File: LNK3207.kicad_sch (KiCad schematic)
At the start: 18 parts, among them U1 LNK3206D

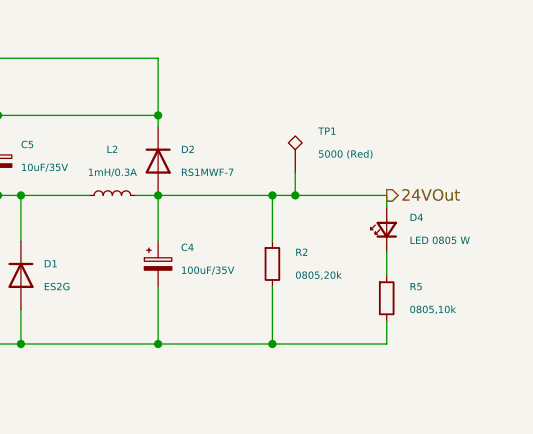
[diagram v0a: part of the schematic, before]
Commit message: [A02] Edited R4, R5
R4 20k -> 10k since nothing else uses 20k
R5 10k -> 510k to reduce D3 LED brightness
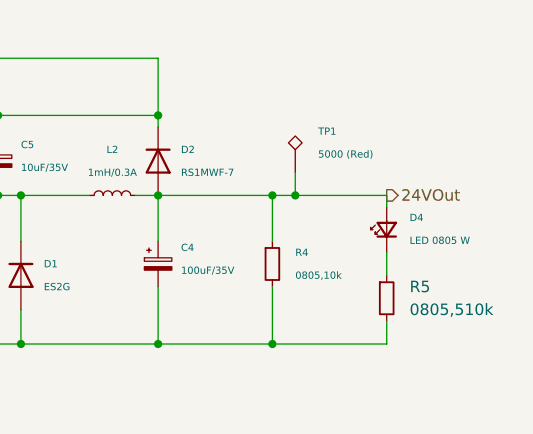
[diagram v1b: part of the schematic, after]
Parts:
- removed R2: 0805,20k, R_0805_2012Metric, symbol jlcpcb-basic-resistor:0805,20k
- removed R5: 0805,10k, R_0805_2012Metric, symbol jlcpcb-basic-resistor:0805,10k
- added R4: 0805,10k, R_0805_2012Metric, symbol jlcpcb-basic-resistor:0805,10k
- added R5: 0805,510k, R_0805_2012Metric, symbol jlcpcb-basic-resistor:0805,510k
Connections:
- net -HV: now also R4.2, R5.2
- net 24VOut: now also R4.1
- net at D4.1 (K): now also R5.1
